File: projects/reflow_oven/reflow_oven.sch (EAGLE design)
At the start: 35 parts, among them IC1 MEGA32-A, IC2 7805DT, IC3 FT232RL, IC4 74HC14D, X1 USB, X2 16.000MHz

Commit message: better layout of board
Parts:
- removed C8: 10uF, adafruit:CPOL-US175TMP-0810
- removed C9: 0.1uF, rcl:C-EUC0805
- removed CN1: (no value), adafruit:DCBARRELPTH
- removed POWERLED: Green, adafruit:LEDCHIP-LED0805
- removed R3: 10k, resistor:R-US_R0805
- removed R4: 150, resistor:R-US_R0805
- removed S1: RESET, switch-omron:10-XX
- removed S2, S3: (no value), switch-omron:10-XX
- added D3: (no value), adafruit:DIODESMA
- added J1: 1X2-3.5MM, adafruit:1X2-3.5MM
- added JP1, JP2: (no value), adafruit:PINHD-1X8CLEANBIG
- added SW1: RST SW, adafruit:SPST_TACT-EVQQ2
- added SW2: D3 SW, adafruit:SPST_TACT-EVQQ2
- added SW3: D2 SW, adafruit:SPST_TACT-EVQQ2
- added U$1: 10k, adafruit:TRIMPOTTC33X
- C5, C6: device rcl:C-EUC0805 -> rcl:CPOL-US085CS-1AR
- C7: value 10uF -> (none); device adafruit:CPOL-US175TMP-0810 -> rcl:CPOL-US085CS-1AR
- IC1: value MEGA32-A -> MEGA8-AI; device atmel:MEGA32-A -> atmel:MEGA8-AI; MPN (none) -> ATMEGA328P-AU; OC_FARNELL (none) -> 1715486; OC_NEWARK (none) -> 68T2935
- X2: value 16.000MHz -> 16MHz
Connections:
- removed net N$1: C5.2, IC1.XTAL2, X2.P$2
- removed net N$11: IC1.(OC2)PD7
- removed net N$17: IC1.(TDI)PC5
- removed net N$18: IC1.(TOSC1)PC6
- removed net N$19: IC1.(TOSC2)PC7
- removed net N$2: C6.2, IC1.XTAL1, X2.P$1
- removed net N$5: POWERLED.C, R4.2
- removed net N$6: IC1.(INT0)PD2
- removed net N$7: IC1.(INT1)PD3
- removed net N$8: IC1.(OC1B)PD4
- removed net VCC: C12.1, C2.1, C3.+, C9.2, IC1.AREF, IC1.AVCC, IC1.VCC, IC1.VCC1, IC1.VCC2, IC3.VCC, IC4P.VCC, R1.2, R2.2, R3.1, R5.1, R6.1, X1.1
- removed net VOUT: C8.+, IC2.VO, POWERLED.A
- new net 4: IC1.PD4(XCK/T0)
- new net 5: IC1.PD5(T1)
- new net 5V: C12.1, C2.1, C3.+, C7.+, IC1.AVCC, IC1.VCC@1, IC1.VCC@2, IC2.VO, IC3.VCC, IC4P.VCC, JP1.2, JP2.7, R1.2, R2.2, R5.1, R6.1, U$1.A, X1.1
- new net 6: IC1.PD6(AIN0)
- new net 7: IC1.PD7(AIN1), JP1.4
- new net A0: IC1.PC0(ADC0)
- new net L3: JP1.3, U$1.S
- new net PWRIN: D3.A, J1.2
- new net XTAL1: C5.+, IC1.PB6(XTAL1/TOSC1), X2.P$2
- new net XTAL2: C6.+, IC1.PB7(XTAL2/TOSC2), X2.P$1
- net 0: now also IC1.PD0(RXD); no longer IC1.(RXD)PD0
- net 1: now also IC1.PD1(TXD); no longer IC1.(TXD)PD1
- net 10: now also IC1.PB2(SS/OC1B), JP2.4; no longer IC1.(AIN0/INT2)PB2
- net 11: now also IC1.PB3(MOSI/OC2), JP2.5; no longer IC1.(AIN1/OC0)PB3
- net 12: now also IC1.PB4(MISO), JP2.6; no longer IC1.(SS)PB4
- net 13: now also IC1.PB5(SCK); no longer IC1.(MOSI)PB5
- net 2: now also IC1.PD2(INT0)
- net 3: now also IC1.PD3(INT1)
- net 8: now also IC1.PB0(ICP), JP1.6; no longer IC1.(T0/XCK)PB0
- net 9: now also IC1.PB1(OC1A), JP2.3; no longer IC1.(T1)PB1
- net A1: now also IC1.PC1(ADC1); no longer IC1.(TDO)PC4
- net A2: now also IC1.PC2(ADC2); no longer IC1.(TMS)PC3
- net A3: now also IC1.PC3(ADC3); no longer IC1.(TCK)PC2
- net A4: now also IC1.PC4(ADC4/SDA); no longer IC1.PC1(SDA)
- net A5: now also IC1.PC5(ADC5/SCL); no longer IC1.PC0(SCL)
- net GND: now also C5.-, C6.-, IC1.GND@2, J1.1, JP1.1, JP1.5, JP2.8, SW1.S, SW1.S1, SW2.P, SW2.P1, SW3.P, SW3.P1, U$1.E; no longer C5.1, C6.1, C8.-, C9.1, CN1.GND, CN1.GNDBREAK, IC1.GND1, IC1.GND2, R4.1, S1.S, S1.S1, S2.P, S2.P1, S3.P, S3.P1
- net N$10: now also IC1.ADC7; no longer IC1.(ICP)PD6
- net N$12: now also SW2.S, SW2.S1; no longer S2.S, S2.S1
- net N$14: now also SW3.S, SW3.S1; no longer S3.S, S3.S1
- net N$9: now also IC1.ADC6; no longer IC1.(OC1A)PD5
- net RESET: now also IC1.PC6(/RESET), SW1.P, SW1.P1; no longer IC1.RESET, R3.2, S1.P, S1.P1
- net VIN: now also D3.C; no longer C7.+, CN1.PWR
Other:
- note removed: "Check These Names"

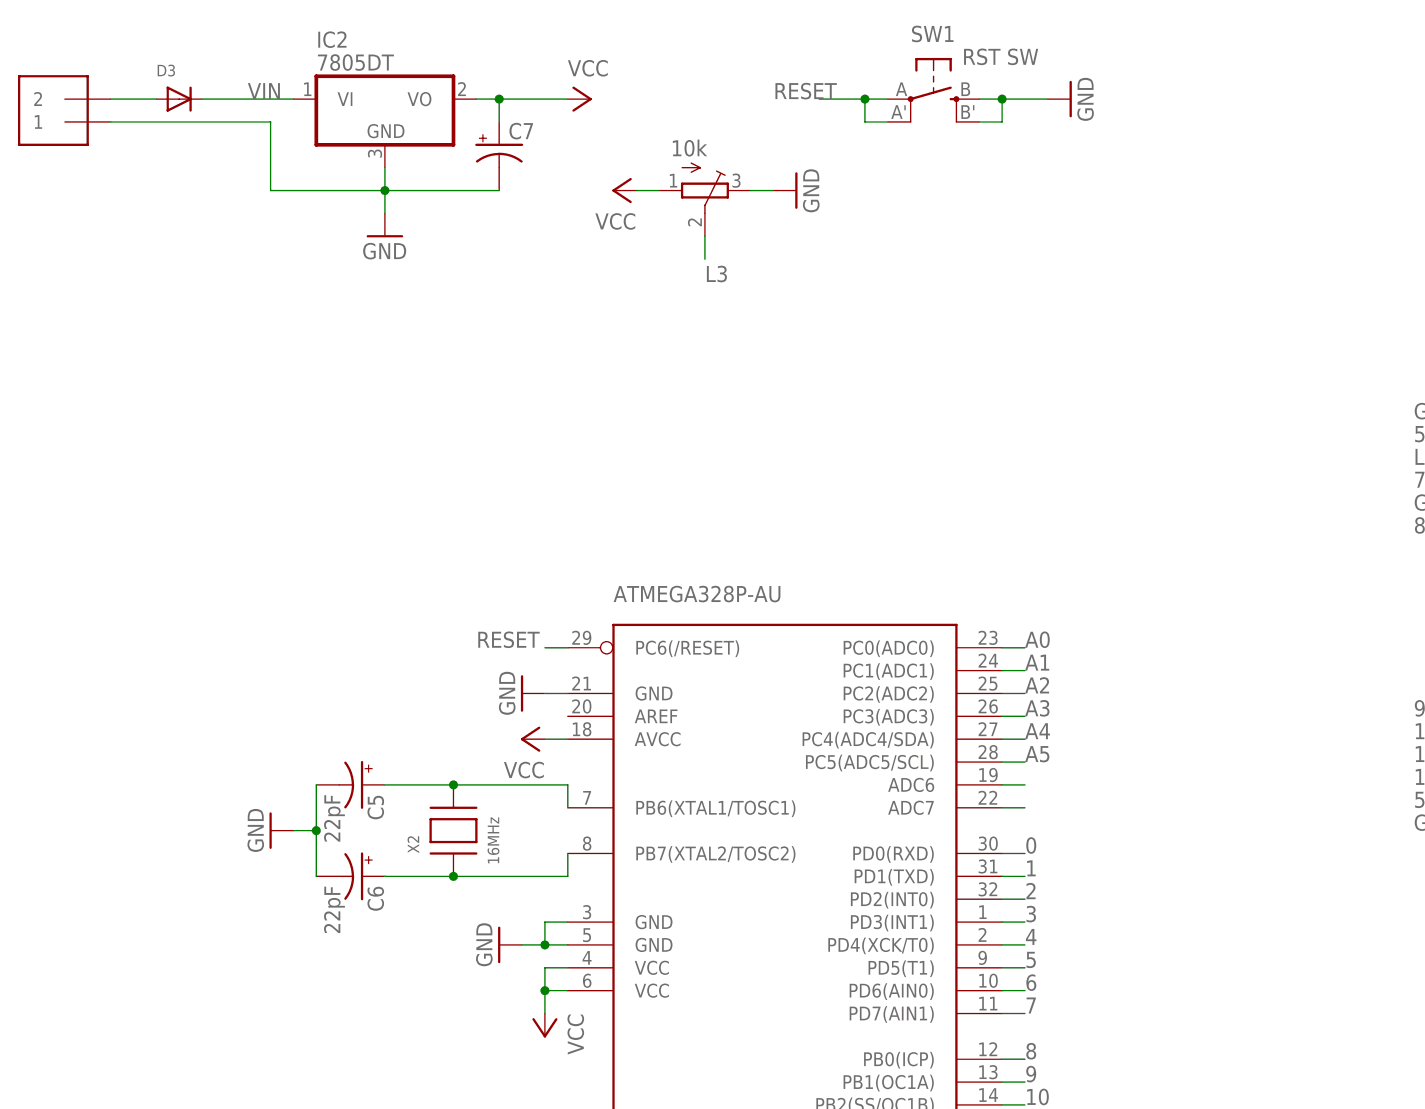
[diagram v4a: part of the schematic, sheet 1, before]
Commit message: changing parts again, now down to 0603 size
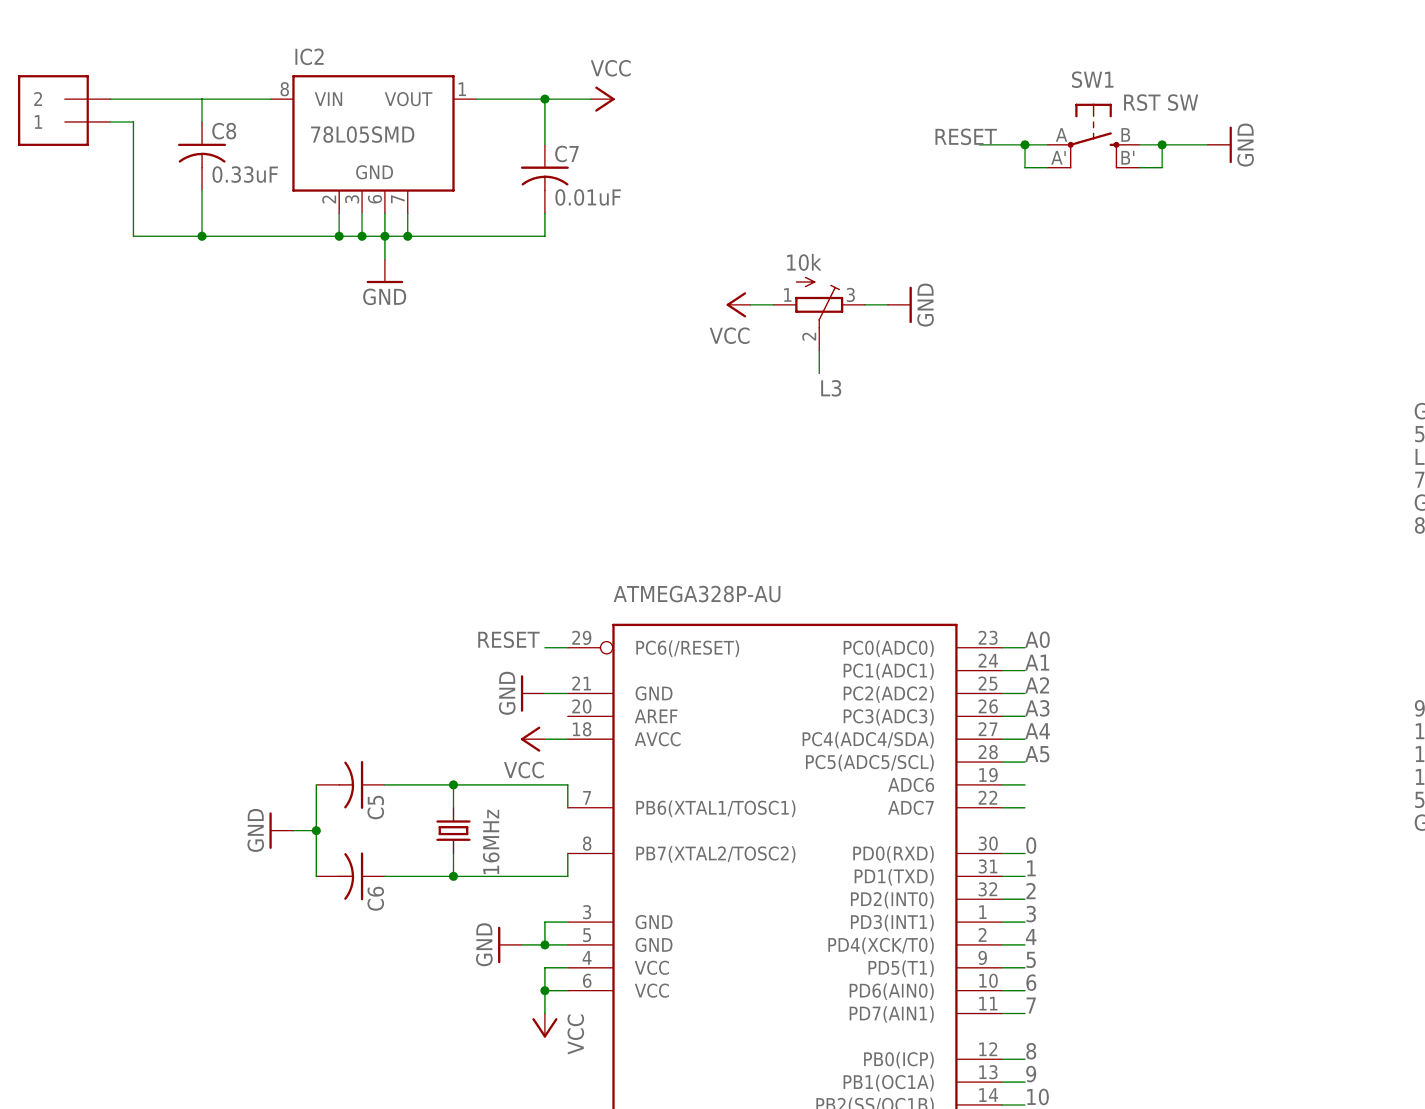
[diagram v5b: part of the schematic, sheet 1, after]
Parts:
- removed C4: 0.1uF, rcl:C-EUC0805
- removed D2: (no value), adafruit:DIODESMA
- removed X2: 16MHz, adafruit:XTALNX8045
- added C8: 0.33uF, rcl:C-USC0603
- added C9: (no value), rcl:C-USC0603
- added Q3: 16MHz, crystal:CRYSTALSM49
- C1: value 0.1uF -> (none); device rcl:C-EUC0805 -> rcl:C-USC0603
- C5, C6: value 22pF -> (none); device rcl:CPOL-US085CS-1AR -> rcl:C-USC0603
- C7: value (none) -> 0.01uF; device rcl:CPOL-US085CS-1AR -> rcl:C-USC0603
- D1, D3: value (none) -> 1N4148; device adafruit:DIODESMA -> adafruit:DIODESOT23_REFLOW
- IC2: value 7805DT -> 78L05SMD; device linear:7805DT -> linear:78L05SMD
- R1, R2: device resistor:R-US_R0805 -> resistor:R-US_R0603
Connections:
- removed net VIN: D3.C, IC2.VI
- net 5V: now also C7.1, IC2G$1.VOUT; no longer C7.+, IC2.VO
- net DTR: now also C9.2; no longer C4.2
- net GND: now also C5.2, C6.2, C7.2, C8.2, IC2G$1.GND@1, IC2G$1.GND@2, IC2G$1.GND@3, IC2G$1.GND@4; no longer C5.-, C6.-, C7.-, IC2.GND
- net N$14: now also D3.A; no longer D2.A
- net N$15: now also D3.C; no longer D2.C
- net PWRIN: now also C8.1, IC2G$1.VIN; no longer D3.A
- net RESET: now also C9.1; no longer C4.1
- net XTAL1: now also C5.1, Q3.2; no longer C5.+, X2.P$2
- net XTAL2: now also C6.1, Q3.1; no longer C6.+, X2.P$1
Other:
- moved on the sheet: SW1
